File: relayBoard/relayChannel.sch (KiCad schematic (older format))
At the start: 9 parts, among them K1 G6S-2, Q1 Q_NMOS_DGS

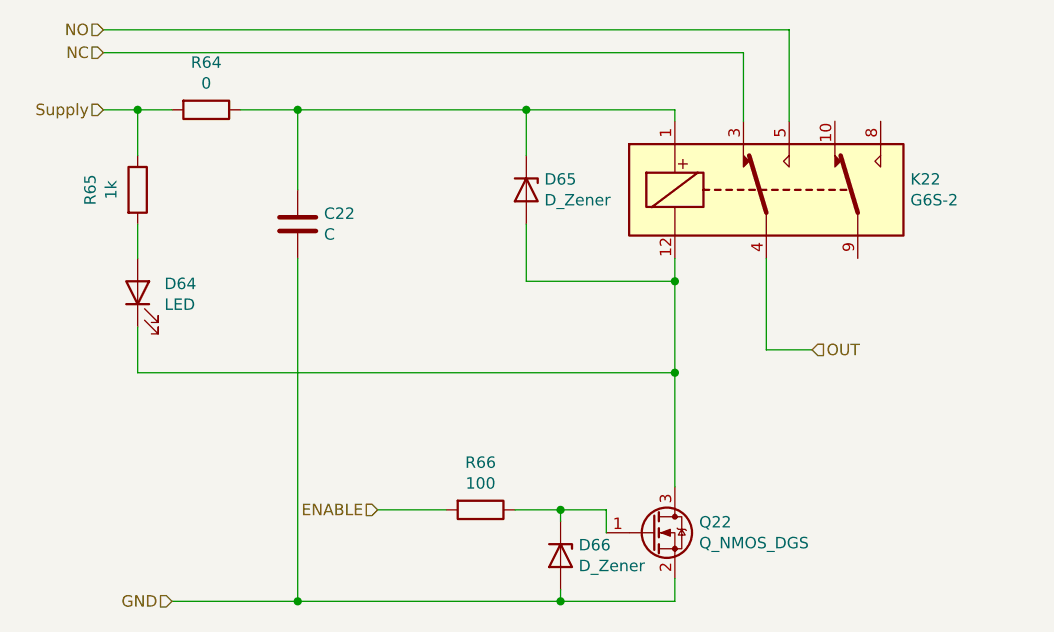
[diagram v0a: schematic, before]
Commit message: Third pass, fixing footprints to match JLC components
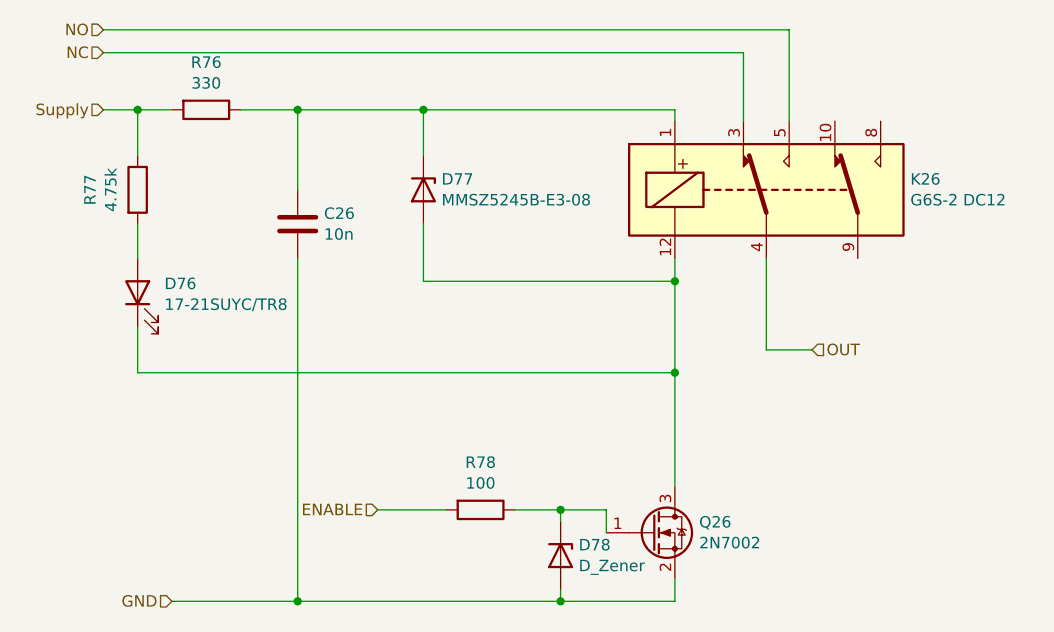
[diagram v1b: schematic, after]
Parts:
- C1: value C -> 10n
- D1: value LED -> 17-21SUYC/TR8
- D2: value D_Zener -> MMSZ5245B-E3-08; footprint Diode_SMD:D_0805_2012Metric -> Diode_SMD:D_SOD-123
- K1: value G6S-2 -> G6S-2 DC12
- Q1: value Q_NMOS_DGS -> 2N7002
- R1: value 0 -> 330
- R2: value 1k -> 4.75k
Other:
- moved on the sheet: D77
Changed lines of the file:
@@
 $Descr A4 11693 8268
 encoding utf-8
-Sheet 23 66
+Sheet 27 66
 Title ""
 Date ""
@@
 AR Path="/5F424711/5CDB6FDA" Ref="Q42"  Part="1"
 AR Path="/5F42471F/5CDB6FDA" Ref="Q?"  Part="1"
-F 0 "Q22" H 5806 5396 50  0000 L CNN
-F 1 "Q_NMOS_DGS" H 5806 5305 50  0000 L CNN
+F 0 "Q26" H 5806 5396 50  0000 L CNN
+F 1 "2N7002" H 5806 5305 50  0000 L CNN
 F 2 "Package_TO_SOT_SMD:SOT-23" H 5800 5450 50  0001 C CNN
 F 3 "~" H 5600 5350 50  0001 C CNN
@@
 AR Path="/5F424711/5CDB82D6" Ref="R124"  Part="1"
 AR Path="/5F42471F/5CDB82D6" Ref="R?"  Part="1"
-F 0 "R64" V 3443 3500 50  0000 C CNN
-F 1 "0" V 3534 3500 50  0000 C CNN
+F 0 "R76" V 3443 3500 50  0000 C CNN
+F 1 "330" V 3534 3500 50  0000 C CNN
 F 2 "Resistor_SMD:R_0603_1608Metric" V 3580 3500 50  0001 C CNN
 F 3 "~" H 3650 3500 50  0001 C CNN
@@
 AR Path="/5F424711/5CDB9938" Ref="R126"  Part="1"
 AR Path="/5F42471F/5CDB9938" Ref="R?"  Part="1"
-F 0 "R66" V 4643 5250 50  0000 C CNN
+F 0 "R78" V 4643 5250 50  0000 C CNN
 F 1 "100" V 4734 5250 50  0000 C CNN
 F 2 "Resistor_SMD:R_0603_1608Metric" V 4780 5250 50  0001 C CNN
@@
 AR Path="/5F424711/5CDF8FE2" Ref="D124"  Part="1"
 AR Path="/5F42471F/5CDF8FE2" Ref="D?"  Part="1"
-F 0 "D64" V 3389 4183 50  0000 R CNN
-F 1 "LED" V 3298 4183 50  0000 R CNN
+F 0 "D76" V 3389 4183 50  0000 R CNN
+F 1 "17-21SUYC/TR8" V 3298 4183 50  0000 R CNN
 F 2 "Resistor_SMD:R_0805_2012Metric" H 3350 4300 50  0001 C CNN
 F 3 "~" H 3350 4300 50  0001 C CNN
@@
 AR Path="/5F424711/5CDFE5C3" Ref="K42"  Part="1"
 AR Path="/5F42471F/5CDFE5C3" Ref="K?"  Part="1"
-F 0 "K22" H 6730 3896 50  0000 L CNN
-F 1 "G6S-2" H 6730 3805 50  0000 L CNN
+F 0 "K26" H 6730 3896 50  0000 L CNN
+F 1 "G6S-2 DC12" H 6730 3805 50  0000 L CNN
 F 2 "Relay_THT:Relay_DPDT_Omron_G6SK-2" H 6750 3800 50  0001 L CNN
 F 3 "http://omronfs.omron.com/en_US/ecb/products/pdf/en-g6s.pdf" H 5900 3850 50  0001 C CNN
@@
 AR Path="/5F424711/5F2F7EF9" Ref="C42"  Part="1"
 AR Path="/5F42471F/5F2F7EF9" Ref="C?"  Part="1"
-F 0 "C22" H 4165 4046 50  0000 L CNN
-F 1 "C" H 4165 3955 50  0000 L CNN
+F 0 "C26" H 4165 4046 50  0000 L CNN
+F 1 "10n" H 4165 3955 50  0000 L CNN
 F 2 "Resistor_SMD:R_0603_1608Metric" H 4088 3850 50  0001 C CNN
 F 3 "~" H 4050 4000 50  0001 C CNN
@@
 AR Path="/5F424711/5F2FEE53" Ref="D126"  Part="1"
 AR Path="/5F42471F/5F2FEE53" Ref="D?"  Part="1"
-F 0 "D66" V 5154 5529 50  0000 L CNN
+F 0 "D78" V 5154 5529 50  0000 L CNN
 F 1 "D_Zener" V 5245 5529 50  0000 L CNN
 F 2 "Diode_SMD:D_0805_2012Metric" H 5200 5450 50  0001 C CNN
@@
 L Device:D_Zener D2
 U 1 1 5F3531C8
-P 5050 3850
+P 4600 3850
 AR Path="/5CDBA1F6/5F3531C8" Ref="D2"  Part="1"
 AR Path="/5F3BDA7F/5F3531C8" Ref="D5"  Part="1"
@@
 AR Path="/5F424711/5F3531C8" Ref="D125"  Part="1"
 AR Path="/5F42471F/5F3531C8" Ref="D?"  Part="1"
-F 0 "D65" V 5004 3929 50  0000 L CNN
-F 1 "D_Zener" V 5095 3929 50  0000 L CNN
-F 2 "Diode_SMD:D_0805_2012Metric" H 5050 3850 50  0001 C CNN
-F 3 "~" H 5050 3850 50  0001 C CNN
-	1    5050 3850
+F 0 "D77" V 4554 3929 50  0000 L CNN
+F 1 "MMSZ5245B-E3-08" V 4645 3929 50  0000 L CNN
+F 2 "Diode_SMD:D_SOD-123" H 4600 3850 50  0001 C CNN
+F 3 "~" H 4600 3850 50  0001 C CNN
+	1    4600 3850
 	0    1    1    0
 $EndComp
-Wire Wire Line
-	5050 3700 5050 3500
-Connection ~ 5050 3500
-Wire Wire Line
-	5050 3500 5700 3500
-Wire Wire Line
-	5050 4000 5050 4250
-Wire Wire Line
-	5050 4250 5700 4250
 Connection ~ 5700 4250
 $Comp
@@
 AR Path="/5F424711/5F355CB2" Ref="R125"  Part="1"
 AR Path="/5F42471F/5F355CB2" Ref="R?"  Part="1"
-F 0 "R65" V 3143 3850 50  0000 C CNN
-F 1 "1k" V 3234 3850 50  0000 C CNN
+F 0 "R77" V 3143 3850 50  0000 C CNN
+F 1 "4.75k" V 3234 3850 50  0000 C CNN
 F 2 "Resistor_SMD:R_0603_1608Metric" V 3280 3850 50  0001 C CNN
 F 3 "~" H 3350 3850 50  0001 C CNN
@@
 	3350 3500 3200 3500
 Wire Wire Line
-	4050 3500 5050 3500
+	4050 3500 4600 3500
 Wire Wire Line
 	5700 4250 5700 4650
@@
 Wire Wire Line
 	5700 4650 5700 5150
+Wire Wire Line
+	4600 3700 4600 3500
+Connection ~ 4600 3500
+Wire Wire Line
+	4600 4250 5700 4250
+Wire Wire Line
+	4600 3500 5700 3500
+Wire Wire Line
+	4600 4000 4600 4250
 $EndSCHEMATC

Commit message: Cuyler's revisions to the relay board
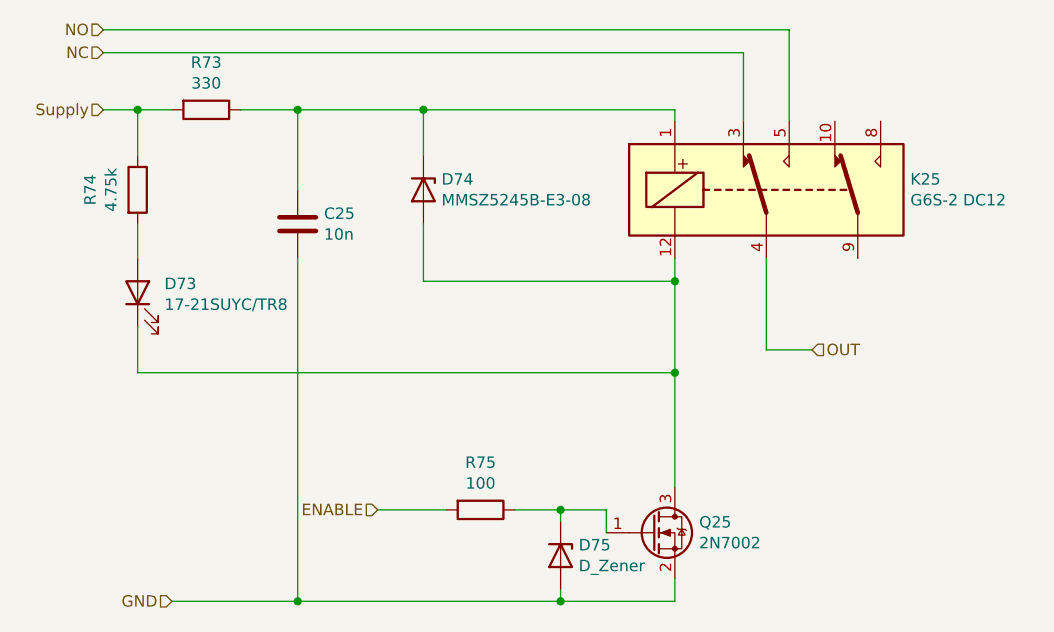
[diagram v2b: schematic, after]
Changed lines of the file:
@@
 EESchema Schematic File Version 4
-EELAYER 30 0
+LIBS:relayBoard-cache
+EELAYER 29 0
 EELAYER END
 $Descr A4 11693 8268
 encoding utf-8
-Sheet 27 66
+Sheet 26 66
 Title ""
 Date ""
@@
 AR Path="/5F424711/5CDB6FDA" Ref="Q42"  Part="1"
 AR Path="/5F42471F/5CDB6FDA" Ref="Q?"  Part="1"
-F 0 "Q26" H 5806 5396 50  0000 L CNN
+F 0 "Q25" H 5806 5396 50  0000 L CNN
 F 1 "2N7002" H 5806 5305 50  0000 L CNN
 F 2 "Package_TO_SOT_SMD:SOT-23" H 5800 5450 50  0001 C CNN
@@
 AR Path="/5F424711/5CDB82D6" Ref="R124"  Part="1"
 AR Path="/5F42471F/5CDB82D6" Ref="R?"  Part="1"
-F 0 "R76" V 3443 3500 50  0000 C CNN
+F 0 "R73" V 3443 3500 50  0000 C CNN
 F 1 "330" V 3534 3500 50  0000 C CNN
 F 2 "Resistor_SMD:R_0603_1608Metric" V 3580 3500 50  0001 C CNN
@@
 AR Path="/5F424711/5CDB9938" Ref="R126"  Part="1"
 AR Path="/5F42471F/5CDB9938" Ref="R?"  Part="1"
-F 0 "R78" V 4643 5250 50  0000 C CNN
+F 0 "R75" V 4643 5250 50  0000 C CNN
 F 1 "100" V 4734 5250 50  0000 C CNN
 F 2 "Resistor_SMD:R_0603_1608Metric" V 4780 5250 50  0001 C CNN
@@
 AR Path="/5F424711/5CDF8FE2" Ref="D124"  Part="1"
 AR Path="/5F42471F/5CDF8FE2" Ref="D?"  Part="1"
-F 0 "D76" V 3389 4183 50  0000 R CNN
+F 0 "D73" V 3389 4183 50  0000 R CNN
 F 1 "17-21SUYC/TR8" V 3298 4183 50  0000 R CNN
 F 2 "Resistor_SMD:R_0805_2012Metric" H 3350 4300 50  0001 C CNN
@@
 AR Path="/5F424711/5CDFE5C3" Ref="K42"  Part="1"
 AR Path="/5F42471F/5CDFE5C3" Ref="K?"  Part="1"
-F 0 "K26" H 6730 3896 50  0000 L CNN
+F 0 "K25" H 6730 3896 50  0000 L CNN
 F 1 "G6S-2 DC12" H 6730 3805 50  0000 L CNN
 F 2 "Relay_THT:Relay_DPDT_Omron_G6SK-2" H 6750 3800 50  0001 L CNN
@@
 AR Path="/5F424711/5F2F7EF9" Ref="C42"  Part="1"
 AR Path="/5F42471F/5F2F7EF9" Ref="C?"  Part="1"
-F 0 "C26" H 4165 4046 50  0000 L CNN
+F 0 "C25" H 4165 4046 50  0000 L CNN
 F 1 "10n" H 4165 3955 50  0000 L CNN
 F 2 "Resistor_SMD:R_0603_1608Metric" H 4088 3850 50  0001 C CNN
@@
 AR Path="/5F424711/5F2FEE53" Ref="D126"  Part="1"
 AR Path="/5F42471F/5F2FEE53" Ref="D?"  Part="1"
-F 0 "D78" V 5154 5529 50  0000 L CNN
+F 0 "D75" V 5154 5529 50  0000 L CNN
 F 1 "D_Zener" V 5245 5529 50  0000 L CNN
 F 2 "Diode_SMD:D_0805_2012Metric" H 5200 5450 50  0001 C CNN
@@
 AR Path="/5F424711/5F3531C8" Ref="D125"  Part="1"
 AR Path="/5F42471F/5F3531C8" Ref="D?"  Part="1"
-F 0 "D77" V 4554 3929 50  0000 L CNN
+F 0 "D74" V 4554 3929 50  0000 L CNN
 F 1 "MMSZ5245B-E3-08" V 4645 3929 50  0000 L CNN
 F 2 "Diode_SMD:D_SOD-123" H 4600 3850 50  0001 C CNN
@@
 AR Path="/5F424711/5F355CB2" Ref="R125"  Part="1"
 AR Path="/5F42471F/5F355CB2" Ref="R?"  Part="1"
-F 0 "R77" V 3143 3850 50  0000 C CNN
+F 0 "R74" V 3143 3850 50  0000 C CNN
 F 1 "4.75k" V 3234 3850 50  0000 C CNN
 F 2 "Resistor_SMD:R_0603_1608Metric" V 3280 3850 50  0001 C CNN

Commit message: updates to connector connections and converter transformer
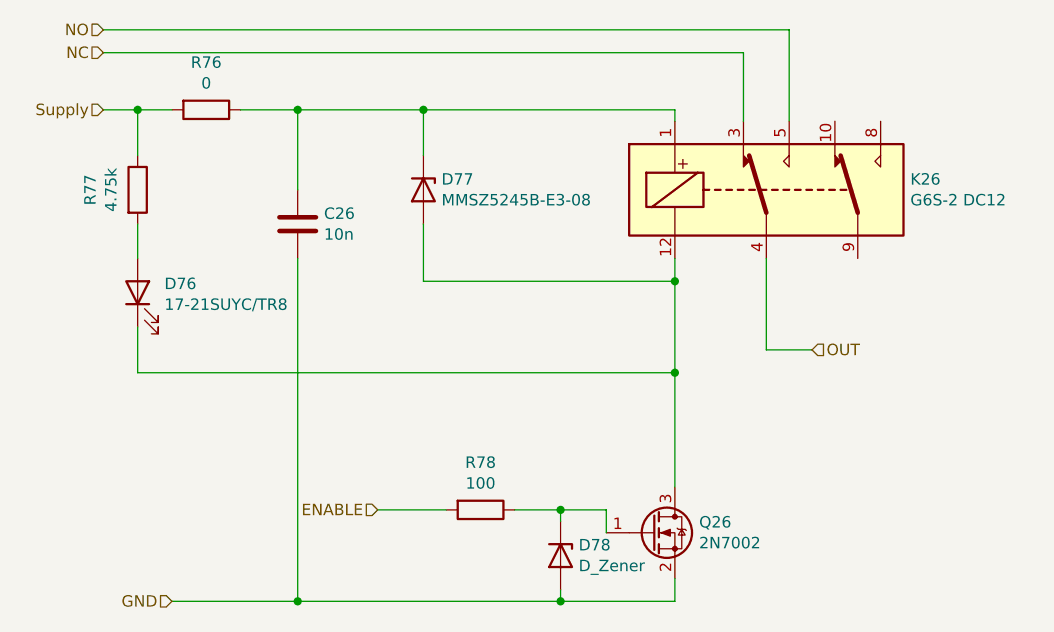
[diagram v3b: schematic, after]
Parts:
- R1: value 330 -> 0
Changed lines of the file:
@@
 EESchema Schematic File Version 4
-LIBS:relayBoard-cache
-EELAYER 29 0
+EELAYER 30 0
 EELAYER END
 $Descr A4 11693 8268
 encoding utf-8
-Sheet 26 66
+Sheet 27 66
 Title ""
 Date ""
@@
 AR Path="/5F424711/5CDB6FDA" Ref="Q42"  Part="1"
 AR Path="/5F42471F/5CDB6FDA" Ref="Q?"  Part="1"
-F 0 "Q25" H 5806 5396 50  0000 L CNN
+F 0 "Q26" H 5806 5396 50  0000 L CNN
 F 1 "2N7002" H 5806 5305 50  0000 L CNN
 F 2 "Package_TO_SOT_SMD:SOT-23" H 5800 5450 50  0001 C CNN
@@
 AR Path="/5F424711/5CDB82D6" Ref="R124"  Part="1"
 AR Path="/5F42471F/5CDB82D6" Ref="R?"  Part="1"
-F 0 "R73" V 3443 3500 50  0000 C CNN
-F 1 "330" V 3534 3500 50  0000 C CNN
+F 0 "R76" V 3443 3500 50  0000 C CNN
+F 1 "0" V 3534 3500 50  0000 C CNN
 F 2 "Resistor_SMD:R_0603_1608Metric" V 3580 3500 50  0001 C CNN
 F 3 "~" H 3650 3500 50  0001 C CNN
@@
 AR Path="/5F424711/5CDB9938" Ref="R126"  Part="1"
 AR Path="/5F42471F/5CDB9938" Ref="R?"  Part="1"
-F 0 "R75" V 4643 5250 50  0000 C CNN
+F 0 "R78" V 4643 5250 50  0000 C CNN
 F 1 "100" V 4734 5250 50  0000 C CNN
 F 2 "Resistor_SMD:R_0603_1608Metric" V 4780 5250 50  0001 C CNN
@@
 AR Path="/5F424711/5CDF8FE2" Ref="D124"  Part="1"
 AR Path="/5F42471F/5CDF8FE2" Ref="D?"  Part="1"
-F 0 "D73" V 3389 4183 50  0000 R CNN
+F 0 "D76" V 3389 4183 50  0000 R CNN
 F 1 "17-21SUYC/TR8" V 3298 4183 50  0000 R CNN
 F 2 "Resistor_SMD:R_0805_2012Metric" H 3350 4300 50  0001 C CNN
@@
 AR Path="/5F424711/5CDFE5C3" Ref="K42"  Part="1"
 AR Path="/5F42471F/5CDFE5C3" Ref="K?"  Part="1"
-F 0 "K25" H 6730 3896 50  0000 L CNN
+F 0 "K26" H 6730 3896 50  0000 L CNN
 F 1 "G6S-2 DC12" H 6730 3805 50  0000 L CNN
 F 2 "Relay_THT:Relay_DPDT_Omron_G6SK-2" H 6750 3800 50  0001 L CNN
@@
 AR Path="/5F424711/5F2F7EF9" Ref="C42"  Part="1"
 AR Path="/5F42471F/5F2F7EF9" Ref="C?"  Part="1"
-F 0 "C25" H 4165 4046 50  0000 L CNN
+F 0 "C26" H 4165 4046 50  0000 L CNN
 F 1 "10n" H 4165 3955 50  0000 L CNN
 F 2 "Resistor_SMD:R_0603_1608Metric" H 4088 3850 50  0001 C CNN
@@
 AR Path="/5F424711/5F2FEE53" Ref="D126"  Part="1"
 AR Path="/5F42471F/5F2FEE53" Ref="D?"  Part="1"
-F 0 "D75" V 5154 5529 50  0000 L CNN
+F 0 "D78" V 5154 5529 50  0000 L CNN
 F 1 "D_Zener" V 5245 5529 50  0000 L CNN
 F 2 "Diode_SMD:D_0805_2012Metric" H 5200 5450 50  0001 C CNN
@@
 AR Path="/5F424711/5F3531C8" Ref="D125"  Part="1"
 AR Path="/5F42471F/5F3531C8" Ref="D?"  Part="1"
-F 0 "D74" V 4554 3929 50  0000 L CNN
+F 0 "D77" V 4554 3929 50  0000 L CNN
 F 1 "MMSZ5245B-E3-08" V 4645 3929 50  0000 L CNN
 F 2 "Diode_SMD:D_SOD-123" H 4600 3850 50  0001 C CNN
@@
 AR Path="/5F424711/5F355CB2" Ref="R125"  Part="1"
 AR Path="/5F42471F/5F355CB2" Ref="R?"  Part="1"
-F 0 "R74" V 3143 3850 50  0000 C CNN
+F 0 "R77" V 3143 3850 50  0000 C CNN
 F 1 "4.75k" V 3234 3850 50  0000 C CNN
 F 2 "Resistor_SMD:R_0603_1608Metric" V 3280 3850 50  0001 C CNN
